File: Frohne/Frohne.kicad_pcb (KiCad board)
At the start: 4 copper layers, 100 x 100 mm, 215 parts, among them J1 ADC IN, J10 Conn_01x20_Socket, J11 SDR ANT, J12 SDR Out, J2 Conn_02x20_Counter_Clockwise, J3 Conn_02x20_Counter_Clockwise, J4 Conn_01x20_Socket, J5 Conn_01x02, J7 Conn_01x01_Pin, J8 BNC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

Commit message: More tuning.
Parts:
- moved R8 1.23 mm to (115.1, 99.9)
- moved C24 0.19 mm to (115.9, 107.2)
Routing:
- net Net-(U7-1B1): track 37.1 -> 51.9 mm
- net Net-(U7-1B2): track 33.6 -> 38.0 mm
- net Net-(U5A-+): track 34.8 -> 38.8 mm
- net Net-(U5B-+): track 39.8 -> 38.0 mm
- net /Q: track 12.7 -> 12.1 mm

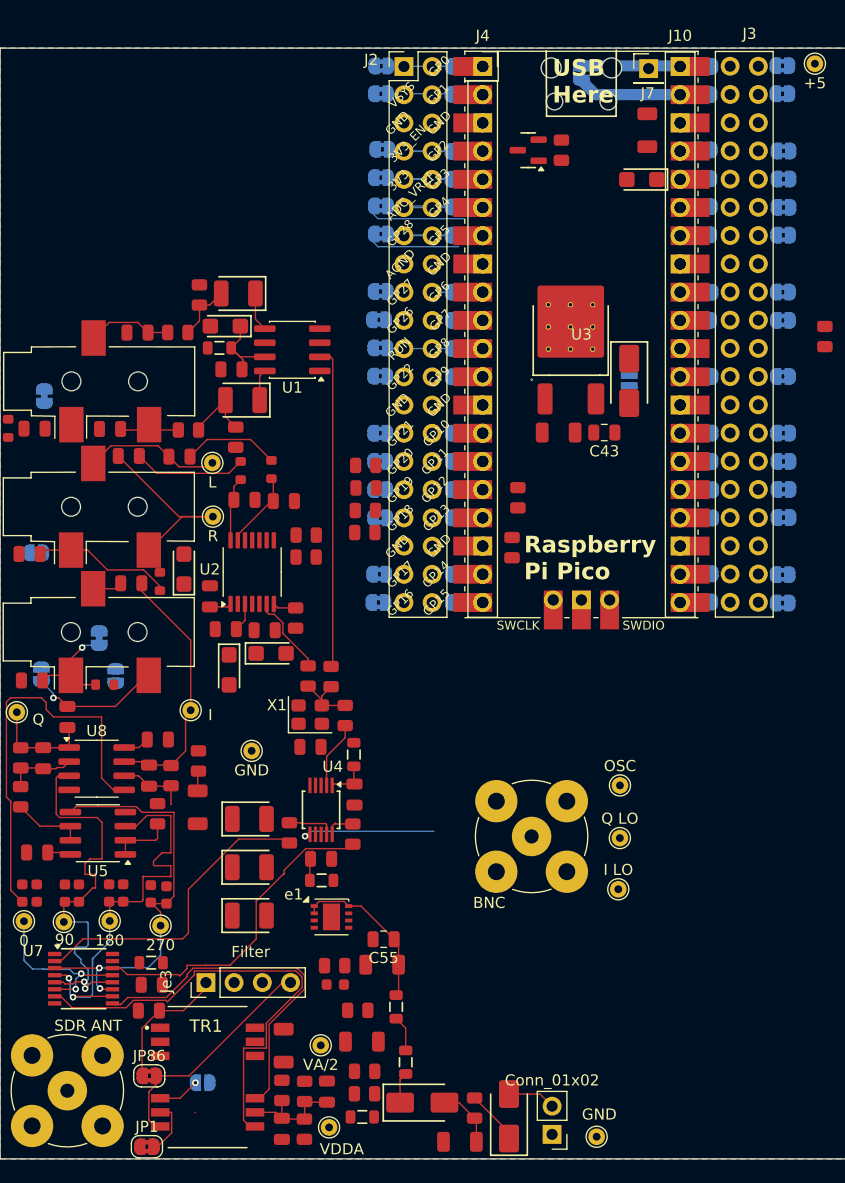
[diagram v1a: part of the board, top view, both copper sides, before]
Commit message: Added some power traces
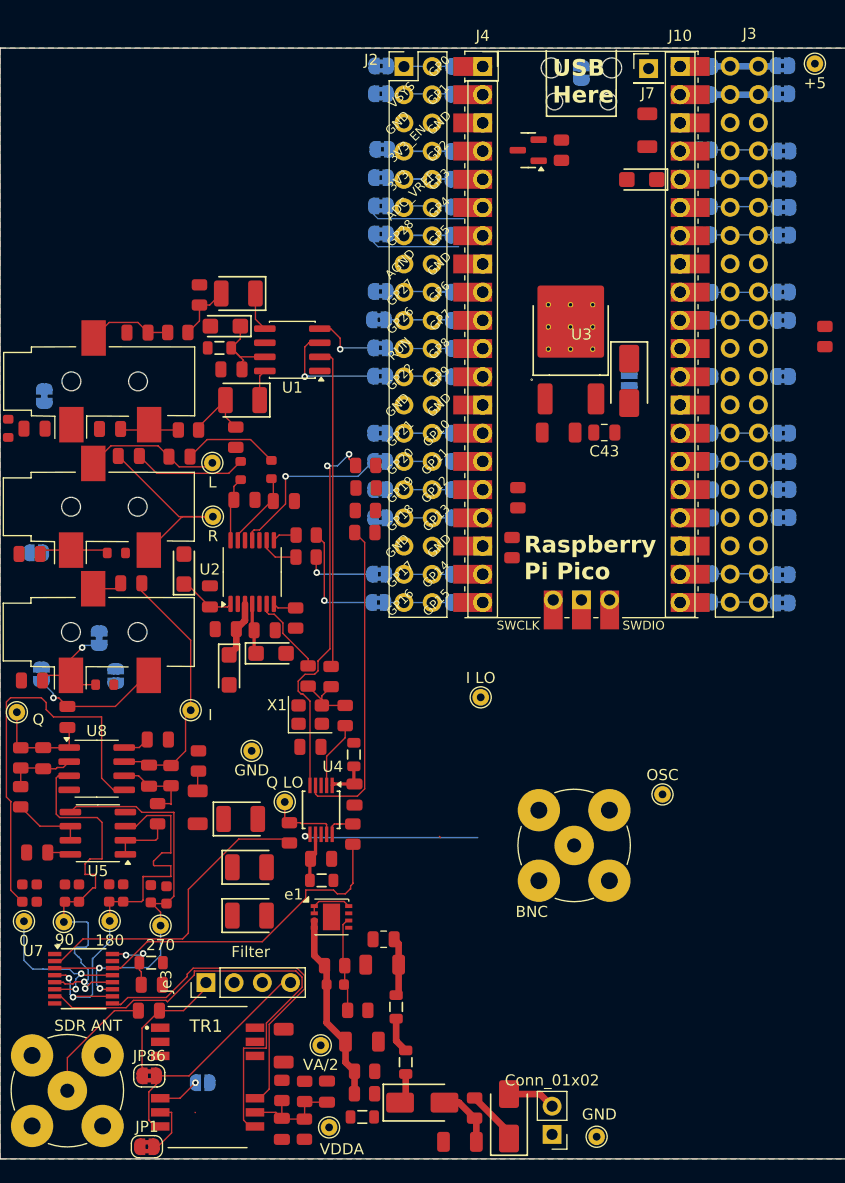
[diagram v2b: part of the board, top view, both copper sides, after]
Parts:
- moved TP4 30.3 mm to (126.6, 98.8)
- moved TP3 21.3 mm to (144.2, 89.4)
- moved R14 4.69 mm to (111.4, 76.4), turned to 0 degrees
- moved TP5 3.91 mm to (160.6, 98.1)
- moved J8 3.91 mm to (152.6, 102.7)
- moved C17 0.79 mm to (122.6, 100.3)
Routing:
- net /OSC_SDA: track 0.00 -> 34.7 mm, vias 0 -> 2
- net /OSC_SCL: track 0.00 -> 29.0 mm
- net Net-(C35-Pad1): track 0.01 -> 17.1 mm
- net /MD1: track 0.00 -> 15.7 mm, vias 0 -> 1
- net +4.7V: track 14.1 -> 0.00 mm
- net Net-(J11-In): track 0.00 -> 11.1 mm
- net /BCK: track 0.00 -> 10.5 mm, vias 0 -> 1
- net Net-(J10-Pin_1): track 10.4 -> 0.00 mm
- net /LRCK: track 0.00 -> 10.3 mm, vias 0 -> 1
- net Net-(e1-SENSE/ADJ): track 0.00 -> 8.62 mm
- net /DATA: track 0.00 -> 6.45 mm, vias 0 -> 1
- net Net-(e4-B): track 12.7 -> 6.29 mm
- net /MCLK: track 0.00 -> 6.20 mm, vias 0 -> 1
- net Net-(U7-VCC): track 0.00 -> 5.89 mm, vias 0 -> 2
- net Net-(J2-Pin_20): track 0.00 -> 5.85 mm
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
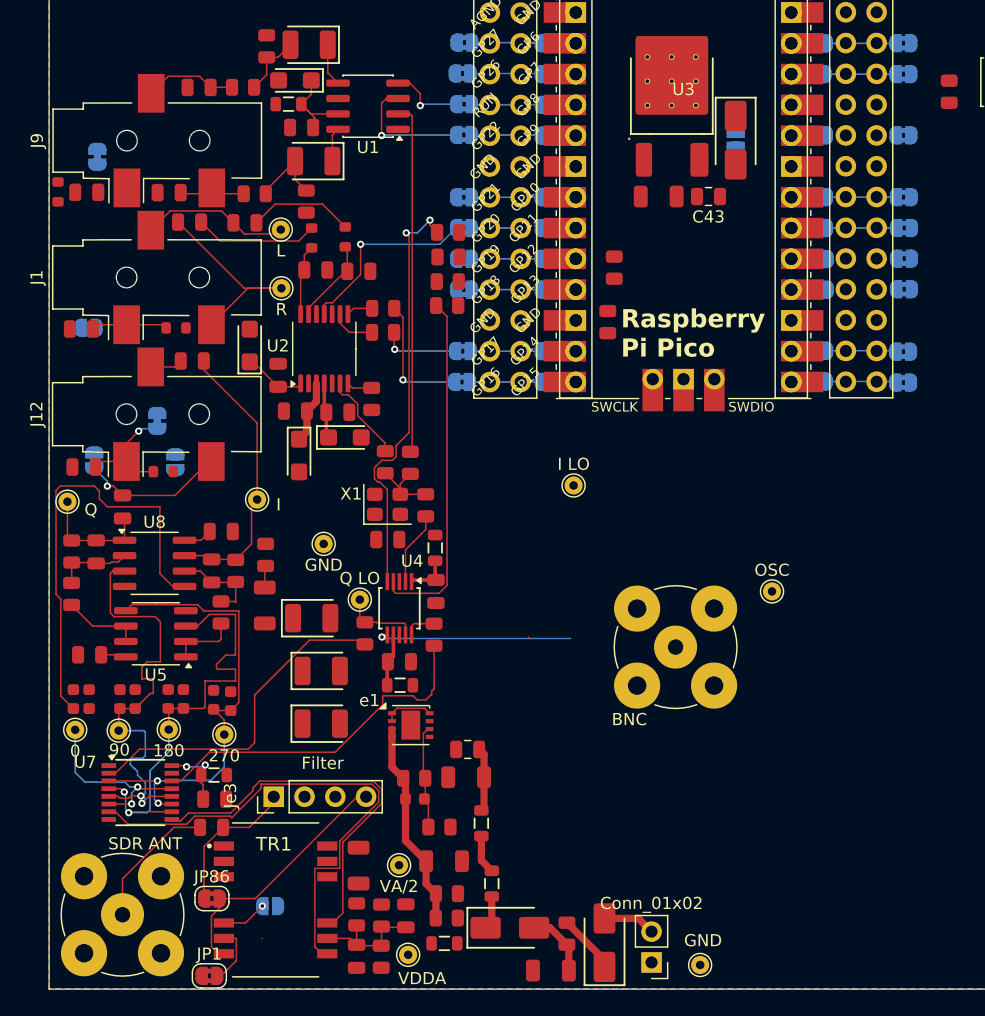
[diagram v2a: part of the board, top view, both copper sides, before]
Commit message: Routing everything now.
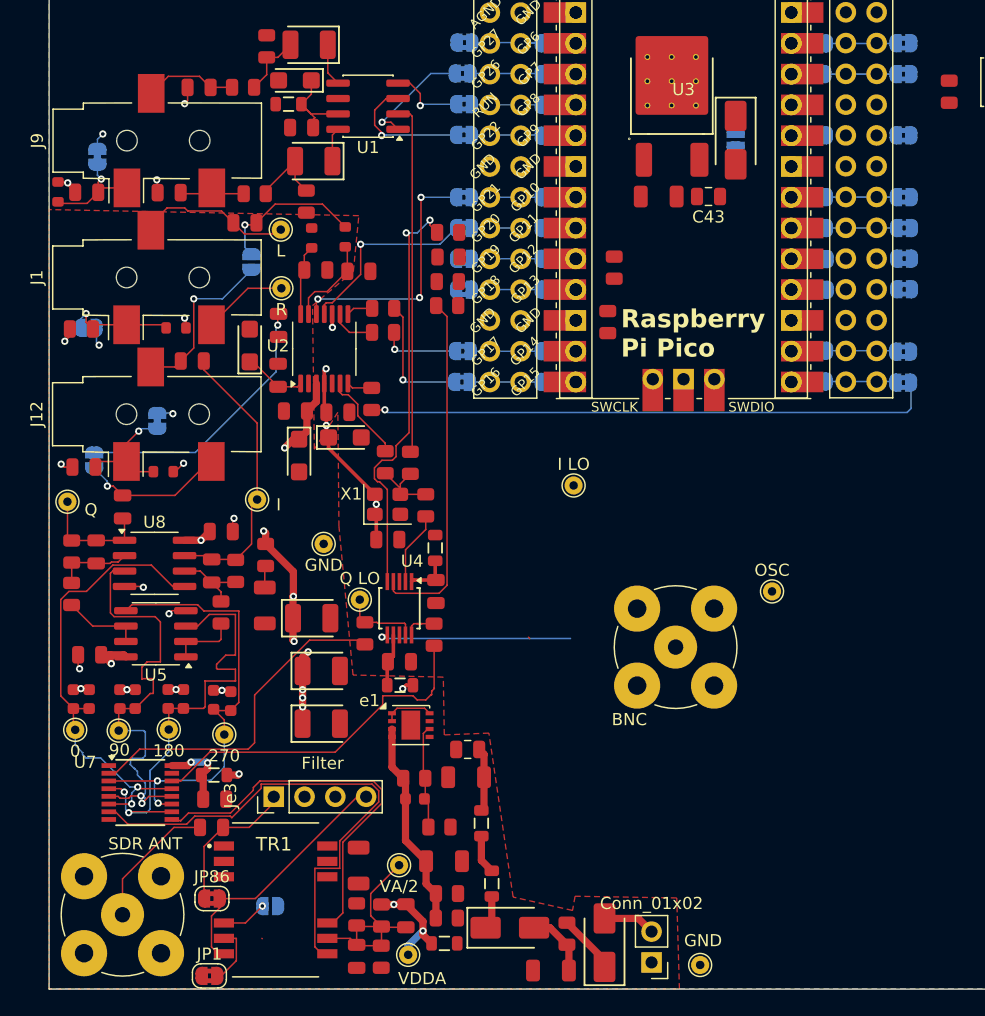
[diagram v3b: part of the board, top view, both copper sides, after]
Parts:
- moved JP18 17.7 mm to (117.6, 71.0)
- moved C4 11.2 mm to (119.9, 76.2), turned to -90 degrees
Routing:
- net /WS: track 0.00 -> 46.9 mm, vias 0 -> 1
- net VDDA: track 9.68 -> 38.2 mm, vias 0 -> 13
- net GND: track 0.33 -> 24.0 mm, vias 0 -> 18
- net /FMT: track 0.00 -> 20.9 mm, vias 0 -> 3
- net +3.3V: track 4.60 -> 18.0 mm, vias 0 -> 5
- net Net-(U7-1B1): track 51.9 -> 39.0 mm
- net Net-(JP19-B): track 10.2 -> 22.6 mm, vias 0 -> 1
- net /I: track 3.04 -> 14.4 mm, vias 0 -> 1
- net Net-(C4-Pad2): track 17.8 -> 7.02 mm
- net /SDIN: track 0.00 -> 9.21 mm, vias 0 -> 1
- net Net-(e3-B): track 0.00 -> 8.79 mm, vias 0 -> 1
- net Net-(TR1-C_RX): track 9.93 -> 18.4 mm
- net Net-(JP18-A): track 8.75 -> 12.5 mm, vias 0 -> 1
- net Net-(e4-B): track 6.29 -> 9.15 mm, vias 0 -> 1
- net Net-(U7-VCC): track 5.89 -> 7.33 mm
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- added copper zone on F.Cu, net VDDA
- added copper zone on In2.Cu, net VDDA
